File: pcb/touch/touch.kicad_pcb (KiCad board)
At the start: 2 copper layers, 99.1 x 25.4 mm, 21 parts, among them J1 HEADER-1x05, Q1 BSS138, Q2 BSS138, SW1 ALARM, SW2 MENU, SW3 SET, U1 AT42QT1070, U2 LP2981-33DBVT

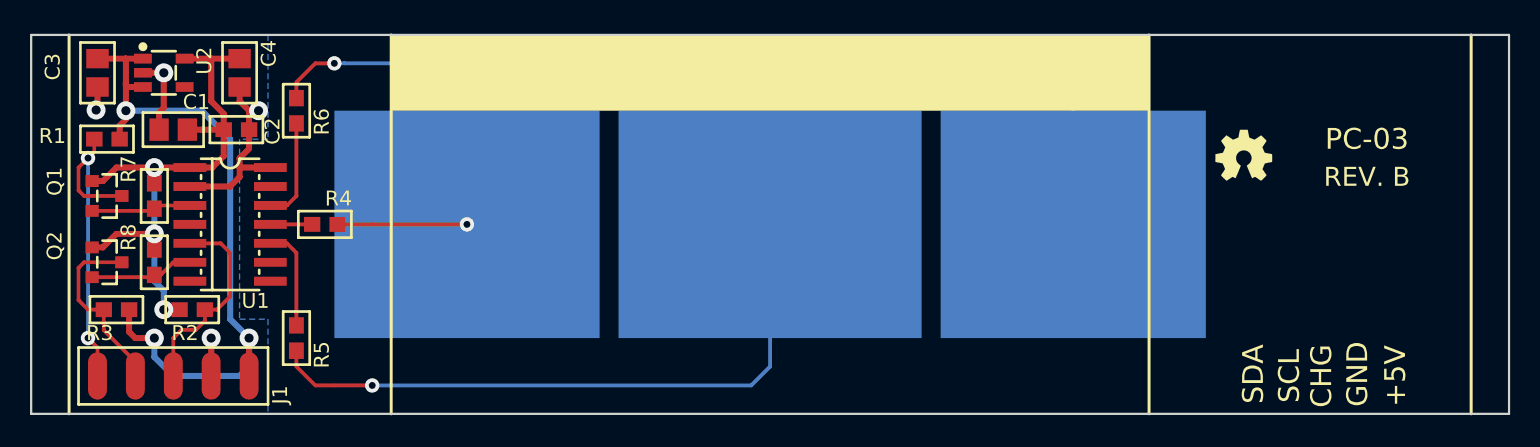
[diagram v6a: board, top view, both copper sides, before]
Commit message: Updated PCB design
+ Completed daughterboard PCB layout.
* Corrected soldermask clerance on front panel pcb.
- Removed input resistor on DIN for RGB lamp board.
* Modified PCB layout for PSU board.
* Updated gerber files.
* Updated schematics pdf, BOM.
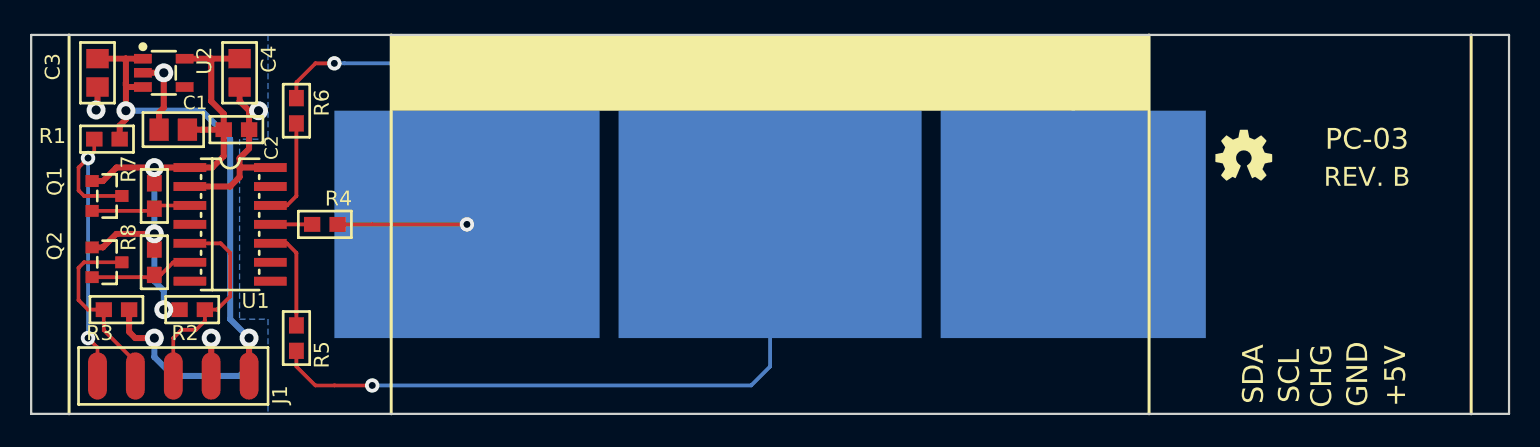
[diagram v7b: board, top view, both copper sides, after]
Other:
- rule pad_to_mask_clearance: 0 -> 0.1524
